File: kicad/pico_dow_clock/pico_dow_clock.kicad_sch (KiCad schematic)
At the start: 33 parts, among them Q1 TEPT4400, Q2 AO3400A, SW1 SW_Push_Dual, U1 AMS1117-3.3

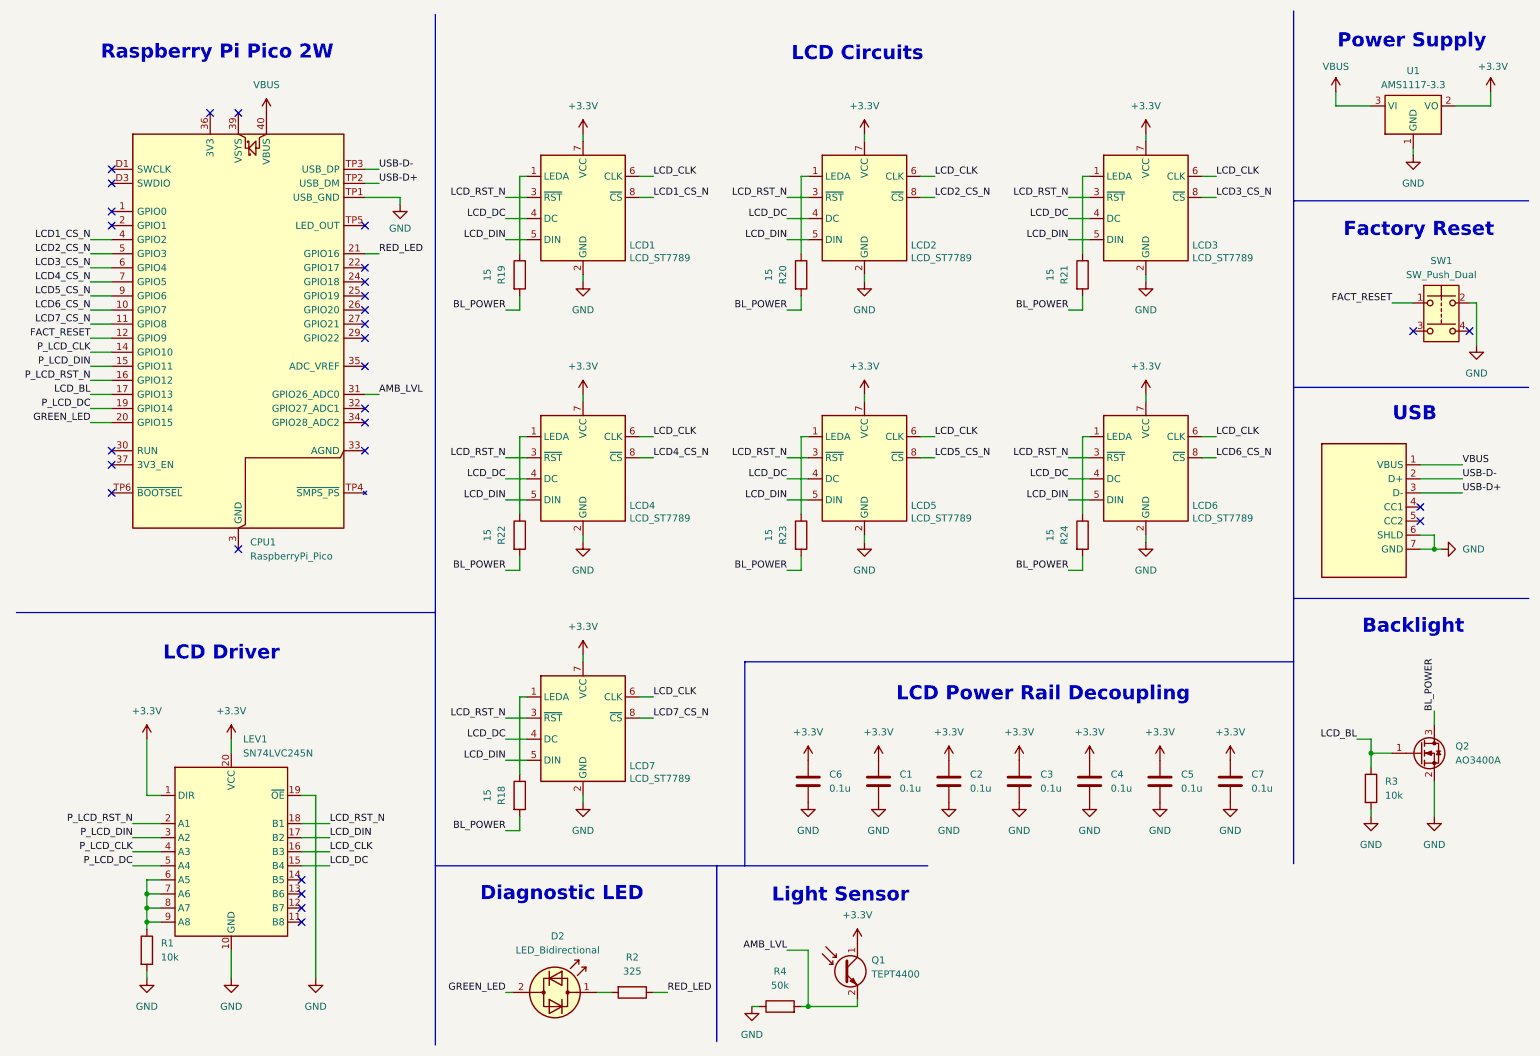
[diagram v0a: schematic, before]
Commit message: New buffer symbols
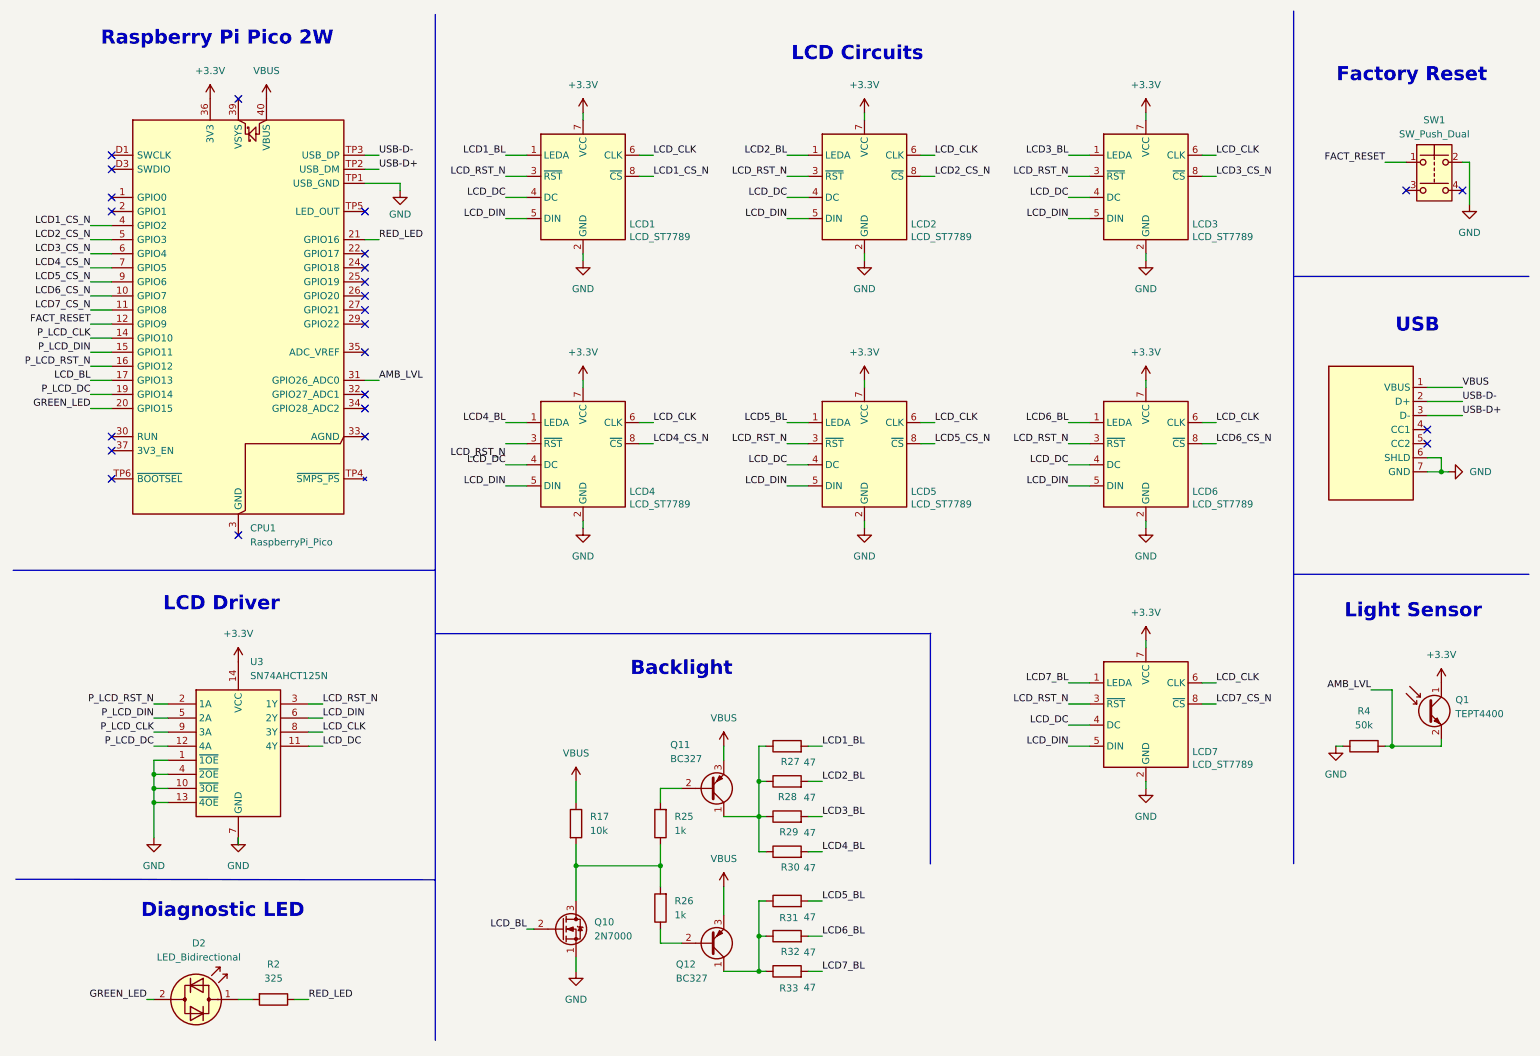
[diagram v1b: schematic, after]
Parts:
- removed C1, C2, C3, C4, C5, C6, C7: 0.1u, symbol Device:C
- removed LEV1: SN74LVC245N, Package_SO:TSSOP-20_4.4x6.5mm_P0.65mm, symbol Logic_LevelTranslator:SN74LVC245APW
- removed Q2: AO3400A, Package_TO_SOT_SMD:SOT-23, symbol Transistor_FET:AO3400A
- removed R1, R3: 10k, symbol Device:R
- removed R18, R19, R20, R21, R22, R23, R24: 15, symbol Device:R
- removed U1: AMS1117-3.3, Package_TO_SOT_SMD:SOT-223-3_TabPin2, symbol Regulator_Linear:AMS1117-3.3
- added Q10: 2N7000, Package_TO_SOT_THT:TO-92_Inline, symbol Transistor_FET:2N7000
- added Q11, Q12: BC327, Package_TO_SOT_THT:TO-92_Inline, symbol Transistor_BJT:BC327
- added R17: 10k, symbol Device:R
- added R25, R26: 1k, symbol Device:R
- added R27, R28, R29, R30, R31, R32, R33: 47, symbol Device:R
- added U3: SN74AHCT125N, symbol local_symbols:SN74AHCT125N
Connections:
- net +3.3V: now also CPU1.36 (3V3), U3.14 (VCC)
- net GND: now also Q10.1 (S), U3.1 (~{1OE}), U3.10 (~{3OE}), U3.13 (~{4OE}), U3.4 (~{2OE}), U3.7 (GND)
- net LCD_BL: now also Q10.2 (G)
- net LCD_CLK: now also U3.8 (3Y)
- net LCD_DC: now also U3.11 (4Y)
- net LCD_DIN: now also U3.6 (2Y)
- net LCD_RST_N: now also U3.3 (1Y); no longer LCD4.3 (~{RST})
- net P_LCD_CLK: now also U3.9 (3A)
- net P_LCD_DC: now also U3.12 (4A)
- net P_LCD_DIN: now also U3.5 (2A)
- net P_LCD_RST_N: now also U3.2 (1A)
- net VBUS: now also Q11.3 (E), Q12.3 (E), R17.1
- net LCD6_BL: now reaches LCD6.1 (LEDA)
- net LCD6_BL: now also R32.2
- net LCD7_BL: now reaches LCD7.1 (LEDA)
- net LCD7_BL: now also R33.2
- net LCD3_BL: now reaches LCD3.1 (LEDA)
- net LCD3_BL: now also R29.2
- net LCD1_BL: now reaches LCD1.1 (LEDA)
- net LCD1_BL: now also R27.2
- net LCD4_BL: now reaches LCD4.1 (LEDA)
- net LCD4_BL: now also R30.2
- net LCD5_BL: now reaches LCD5.1 (LEDA)
- net LCD5_BL: now also R31.2
- net LCD2_BL: now reaches LCD2.1 (LEDA)
- net LCD2_BL: now also R28.2
- new net: Q11.1 (C), R27.1, R28.1, R29.1, R30.1
- new net: Q10.3 (D), R17.2, R25.1, R26.2
- new net: Q11.2 (B), R25.2
- new net: Q12.1 (C), R31.1, R32.1, R33.1
- new net: Q12.2 (B), R26.1
- no-connect marks 29 -> 24
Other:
- note removed: "LCD Power Rail Decoupling"
- note removed: "Power Supply"
- moved on the sheet: CPU1, D2, LCD4, Q1, R2, R4, SW1

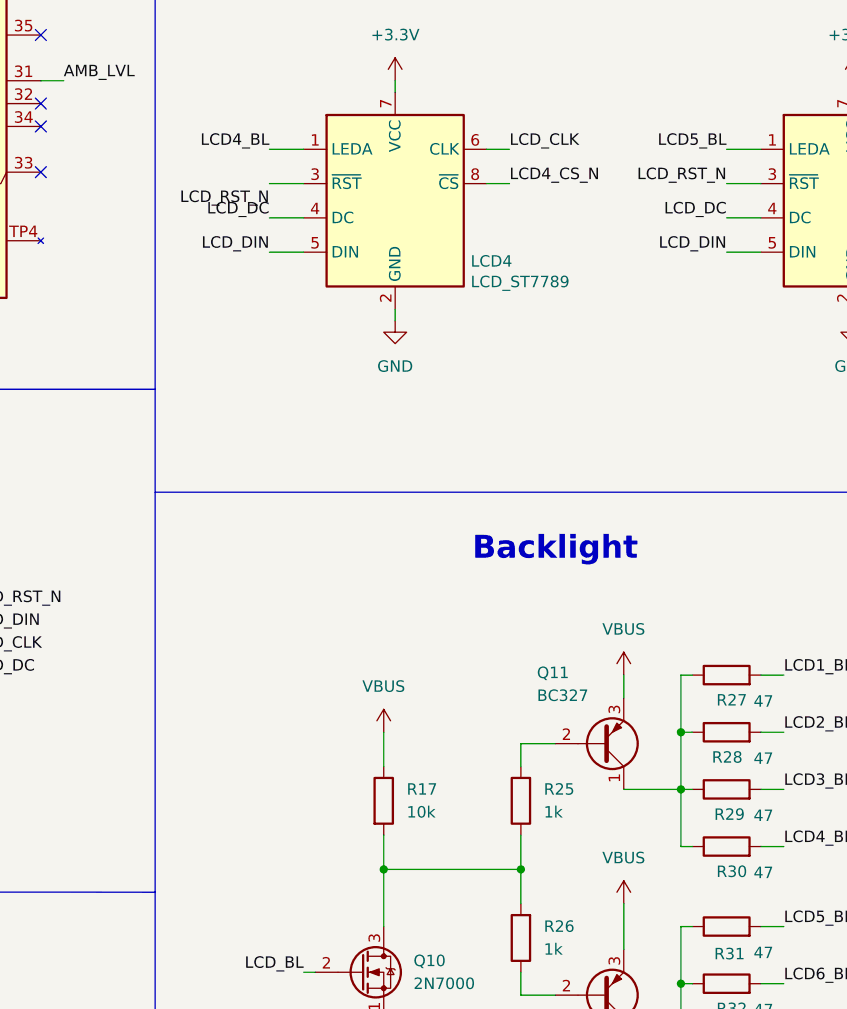
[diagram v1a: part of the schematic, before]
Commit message: ERC error fixes
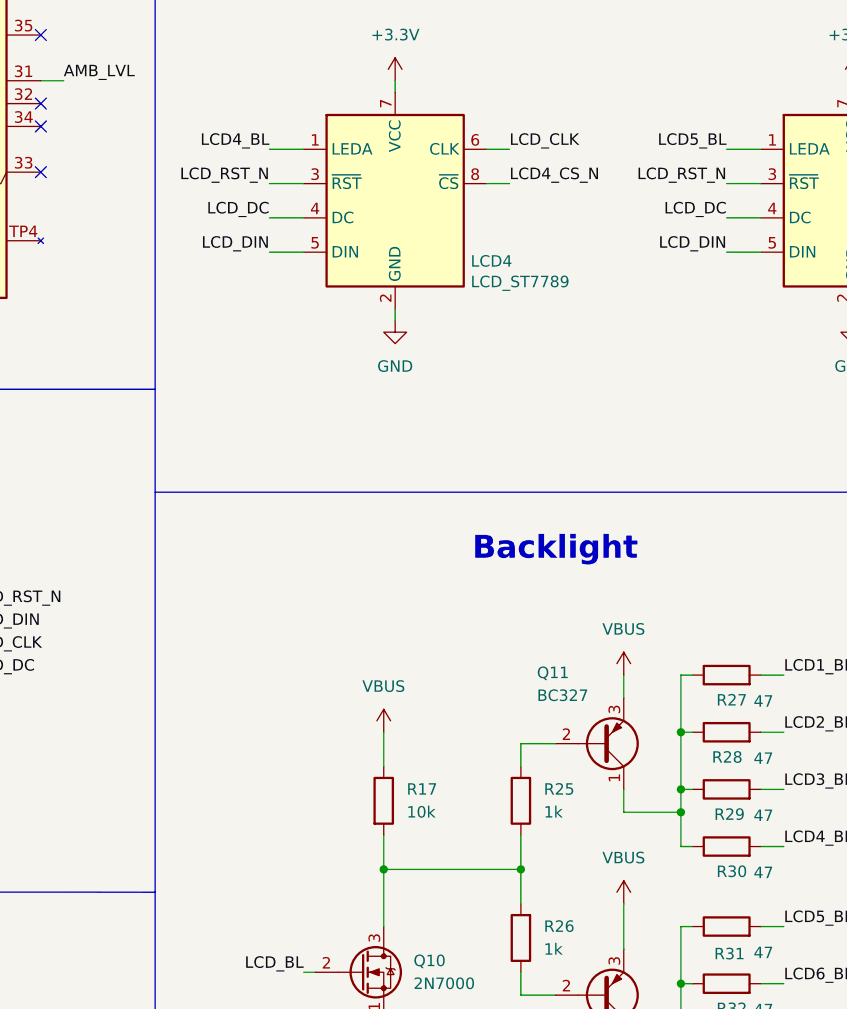
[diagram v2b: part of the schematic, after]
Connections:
- net LCD_RST_N: now also LCD4.3 (~{RST})
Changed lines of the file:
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@@
 	)
 	(junction
+		(at 146.05 160.02)
+		(diameter 0)
+		(color 0 0 0 0)
+	)
+	(junction
 		(at 36.83 149.86)
 		(diameter 0)
@@
 	(wire
 		(pts
-			(xy 139.7 157.48) (xy 146.05 157.48)
-		)
-		(stroke
-			(width 0)
-			(type default)
-		)
-	)
-	(wire
-		(pts
 			(xy 201.93 140.97) (xy 205.74 140.97)
 		)
@@
 	(wire
 		(pts
+			(xy 146.05 160.02) (xy 146.05 163.83)
+		)
+		(stroke
+			(width 0)
+			(type default)
+		)
+	)
+	(wire
+		(pts
 			(xy 215.9 55.88) (xy 215.9 57.15)
 		)
@@
 	(wire
 		(pts
+			(xy 139.7 157.48) (xy 139.7 160.02)
+		)
+		(stroke
+			(width 0)
+			(type default)
+		)
+	)
+	(wire
+		(pts
 			(xy 260.35 144.78) (xy 269.24 144.78)
 		)
@@
 	(wire
 		(pts
-			(xy 146.05 157.48) (xy 146.05 163.83)
+			(xy 146.05 157.48) (xy 146.05 160.02)
 		)
 		(stroke
@@
 		)
 	)
+	(wire
+		(pts
+			(xy 139.7 160.02) (xy 146.05 160.02)
+		)
+		(stroke
+			(width 0)
+			(type default)
+		)
+	)
 	(label "LCD3_BL"
 		(at 157.48 157.48 0)
@@
 	)
 	(label "LCD_RST_N"
-		(at 100.33 92.71 180)
+		(at 100.33 90.17 180)
 		(effects
 			(font
@@
 	(group ""
 		(members "004f0bf2-ecf4-4f78-b933-1d15b2f09ceb" "023ce0f6-ed09-4d2e-b819-47b201ebf578"
-			"051ef6e9-b5e9-43e1-95ef-ee2527077fb0" "0785f753-4ed9-4472-bca6-172484618d90"
-			"09416ce0-010c-4e4a-a8e7-4a55bb6d260d" "0bcdb871-00f5-47c3-82a7-ed2ed2ca5f59"
-			"0fd0c9c6-7ea6-4018-8480-9d46c24fe936" "1021274e-e6a6-483d-b36f-28925353436f"
-			"16c9ad13-d9ee-4591-a434-3e3c366d8679" "21700bc1-ed02-4108-8daa-dd590d161f34"
-			"27fde1cc-505b-4e77-9463-a57f0fc6e798" "2841f079-befe-4285-a7b2-56aff35cb5ff"
-			"28eb840f-f699-4789-90ff-2d4ad53098b2" "2c4f500b-ad39-4198-b859-375b291c8196"
-			"304285b5-fc98-4ac7-8408-20b5a269d587" "3b75d045-b3b9-4b8c-9e5c-6302ec49163f"
+			"051ef6e9-b5e9-43e1-95ef-ee2527077fb0" "09416ce0-010c-4e4a-a8e7-4a55bb6d260d"
+			"0bcdb871-00f5-47c3-82a7-ed2ed2ca5f59" "0fd0c9c6-7ea6-4018-8480-9d46c24fe936"
+			"1021274e-e6a6-483d-b36f-28925353436f" "16c9ad13-d9ee-4591-a434-3e3c366d8679"
+			"21700bc1-ed02-4108-8daa-dd590d161f34" "27fde1cc-505b-4e77-9463-a57f0fc6e798"
+			"2841f079-befe-4285-a7b2-56aff35cb5ff" "28eb840f-f699-4789-90ff-2d4ad53098b2"
+			"2c4f500b-ad39-4198-b859-375b291c8196" "304285b5-fc98-4ac7-8408-20b5a269d587"
+			"3b65cf8d-9cf7-4a30-a3cf-668644ffb07e" "3b75d045-b3b9-4b8c-9e5c-6302ec49163f"
 			"4160baff-26b6-4b49-a0d4-129c547ed35e" "42b77b07-9c7b-41da-9f5f-aeb103d9c8c1"
 			"42e943d2-22a4-4461-a115-7c790b4dec78" "439b04fc-3243-47d0-b52f-64e9eb300b72"
@@
 			"5050f806-a55d-4892-b585-24932e4715d0" "52f5e293-2432-4144-9f4a-7b9e1ad42895"
 			"583397f3-23e2-449b-9ef2-3220d3f1ef6c" "5fde242d-f003-4796-807f-b71767652cbd"
-			"68846203-3798-44ea-8f2f-c95d920116b4" "6be4a454-007a-44dd-b8d6-aaeb58c8ab92"
-			"6c0c96e0-15cd-4ab3-9e10-4ab6e7f82a70" "6e69dede-abff-496f-bd1e-2c217fe26e52"
-			"7020d23b-6479-4aac-bca7-aabc03594cec" "7de08688-95ac-4bba-89d0-a7245c8e34a8"
-			"7ffdc01f-fa08-4c62-9001-aa691e6e93d8" "81842849-9f7c-483b-9ba0-7d4cb2400a03"
-			"81943797-0d42-4dcb-bfca-92f125cc4dda" "83bc83e9-b053-45fc-b2d6-20378007d760"
-			"8ecf8f10-930a-4241-84d3-df60f931eb07" "92ab04c2-22c7-4b66-a5cf-dba6d1cc4acf"
+			"6061a199-f78f-4027-a25d-6844b56ecbbf" "68846203-3798-44ea-8f2f-c95d920116b4"
+			"6be4a454-007a-44dd-b8d6-aaeb58c8ab92" "6c0c96e0-15cd-4ab3-9e10-4ab6e7f82a70"
+			"6e69dede-abff-496f-bd1e-2c217fe26e52" "7020d23b-6479-4aac-bca7-aabc03594cec"
+			"7de08688-95ac-4bba-89d0-a7245c8e34a8" "7ffdc01f-fa08-4c62-9001-aa691e6e93d8"
+			"81842849-9f7c-483b-9ba0-7d4cb2400a03" "81943797-0d42-4dcb-bfca-92f125cc4dda"
+			"83bc83e9-b053-45fc-b2d6-20378007d760" "8ecf8f10-930a-4241-84d3-df60f931eb07"
+			"92ab04c2-22c7-4b66-a5cf-dba6d1cc4acf" "94ebe9b7-103e-4944-9f9a-8a24edd03dce"
 			"a33959ef-0966-4a51-839f-b58f251e8de9" "a4bf2cde-fd27-4c20-b36b-f7655d3b248b"
 			"a7b330f7-5f3c-4f10-ae28-0ba65276a24e" "ab209053-8947-46a8-a447-d9817a0db76a"
@@
 			"f3e4da67-9b6a-4586-909d-d94243e72968" "f6a81df1-1d36-4b02-b741-ac4dfdacc6ea"
 			"fb74be94-2792-4a1f-be81-61817916b496" "fda1eae7-40cd-4973-9919-4fec27b4e566"
+			"ff7e2fe1-82ce-4095-8bb4-42afc020b0b9"
 		)
 	)
@@
 		)
 	)
-	(group ""
-		(members "02fdeb7a-6e61-4f8a-9f7d-1c856b68b4a0" "09b11e5a-099e-4504-8bb9-55f490a2ba26"
-			"12f358b9-6add-461d-9e3c-338d794c83cf" "215fd9cb-e540-479d-9d76-8d015c415d3d"
-			"4d79d525-f07a-4a20-8443-8916c4394c70" "6132c717-d2c9-4c85-b3f2-811fc5f4208e"
-			"6c611af4-6527-4cc1-97b2-f939a55fef65" "70aad0f0-1dcd-4559-9d42-bfcc03a8de31"
-			"77bf1413-a7ee-4eb6-8628-7a74e82addfe" "82723b60-a528-4539-8306-74959a1d316c"
-			"89fa6ecd-2837-4a35-a6b6-d3df73e970bc" "8f9cc0da-ce52-4630-814d-6d3d584356c8"
-			"91833546-208c-4a04-a36b-3a98d6846521" "9bd0186b-7968-4b89-b502-d2de668975c1"
-			"ac7c58dd-481f-4e21-899a-168c97de0ea4" "d4d5e33b-828a-4921-8e67-9901e9b093a0"
-			"f822bd63-d6c7-49bc-b22b-03e48a41cb10"
-		)
-	)

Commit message: Assigned resistor footprints
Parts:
- R17, R2, R25, R26, R27, R28, R29, R30, R31, R32, R33, R4: footprint (none) -> Resistor_THT:R_Axial_DIN0207_L6.3mm_D2.5mm_P7.62mm_Horizontal
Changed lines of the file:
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@@
 			)
 		)
-		(property "Footprint" ""
+		(property "Footprint" "Resistor_THT:R_Axial_DIN0207_L6.3mm_D2.5mm_P7.62mm_Horizontal"
 			(at 58.42 188.722 90)
 			(hide yes)
@@
 			)
 		)
-		(property "Footprint" ""
+		(property "Footprint" "Resistor_THT:R_Axial_DIN0207_L6.3mm_D2.5mm_P7.62mm_Horizontal"
 			(at 151.13 165.608 90)
 			(hide yes)
@@
 			)
 		)
-		(property "Footprint" ""
+		(property "Footprint" "Resistor_THT:R_Axial_DIN0207_L6.3mm_D2.5mm_P7.62mm_Horizontal"
 			(at 151.13 159.258 90)
 			(hide yes)
@@
 			)
 		)
-		(property "Footprint" ""
+		(property "Footprint" "Resistor_THT:R_Axial_DIN0207_L6.3mm_D2.5mm_P7.62mm_Horizontal"
 			(at 130.048 158.75 90)
 			(hide yes)
@@
 			)
 		)
-		(property "Footprint" ""
+		(property "Footprint" "Resistor_THT:R_Axial_DIN0207_L6.3mm_D2.5mm_P7.62mm_Horizontal"
 			(at 151.13 180.848 90)
 			(hide yes)
@@
 			)
 		)
-		(property "Footprint" ""
+		(property "Footprint" "Resistor_THT:R_Axial_DIN0207_L6.3mm_D2.5mm_P7.62mm_Horizontal"
 			(at 151.13 152.908 90)
 			(hide yes)
@@
 			)
 		)
-		(property "Footprint" ""
+		(property "Footprint" "Resistor_THT:R_Axial_DIN0207_L6.3mm_D2.5mm_P7.62mm_Horizontal"
 			(at 151.13 146.558 90)
 			(hide yes)
@@
 			)
 		)
-		(property "Footprint" ""
+		(property "Footprint" "Resistor_THT:R_Axial_DIN0207_L6.3mm_D2.5mm_P7.62mm_Horizontal"
 			(at 151.13 187.198 90)
 			(hide yes)
@@
 			)
 		)
-		(property "Footprint" ""
+		(property "Footprint" "Resistor_THT:R_Axial_DIN0207_L6.3mm_D2.5mm_P7.62mm_Horizontal"
 			(at 255.27 146.558 90)
 			(hide yes)
@@
 			)
 		)
-		(property "Footprint" ""
+		(property "Footprint" "Resistor_THT:R_Axial_DIN0207_L6.3mm_D2.5mm_P7.62mm_Horizontal"
 			(at 111.252 158.75 90)
 			(hide yes)
@@
 			)
 		)
-		(property "Footprint" ""
+		(property "Footprint" "Resistor_THT:R_Axial_DIN0207_L6.3mm_D2.5mm_P7.62mm_Horizontal"
 			(at 151.13 174.498 90)
 			(hide yes)
@@
 			)
 		)
-		(property "Footprint" ""
+		(property "Footprint" "Resistor_THT:R_Axial_DIN0207_L6.3mm_D2.5mm_P7.62mm_Horizontal"
 			(at 130.048 173.99 90)
 			(hide yes)
